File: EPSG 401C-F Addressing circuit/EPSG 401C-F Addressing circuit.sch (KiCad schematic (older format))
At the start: 4 parts, among them J1 Conn_01x16_Female, U1 74LS138, U2 74LS138, U3 74LS138

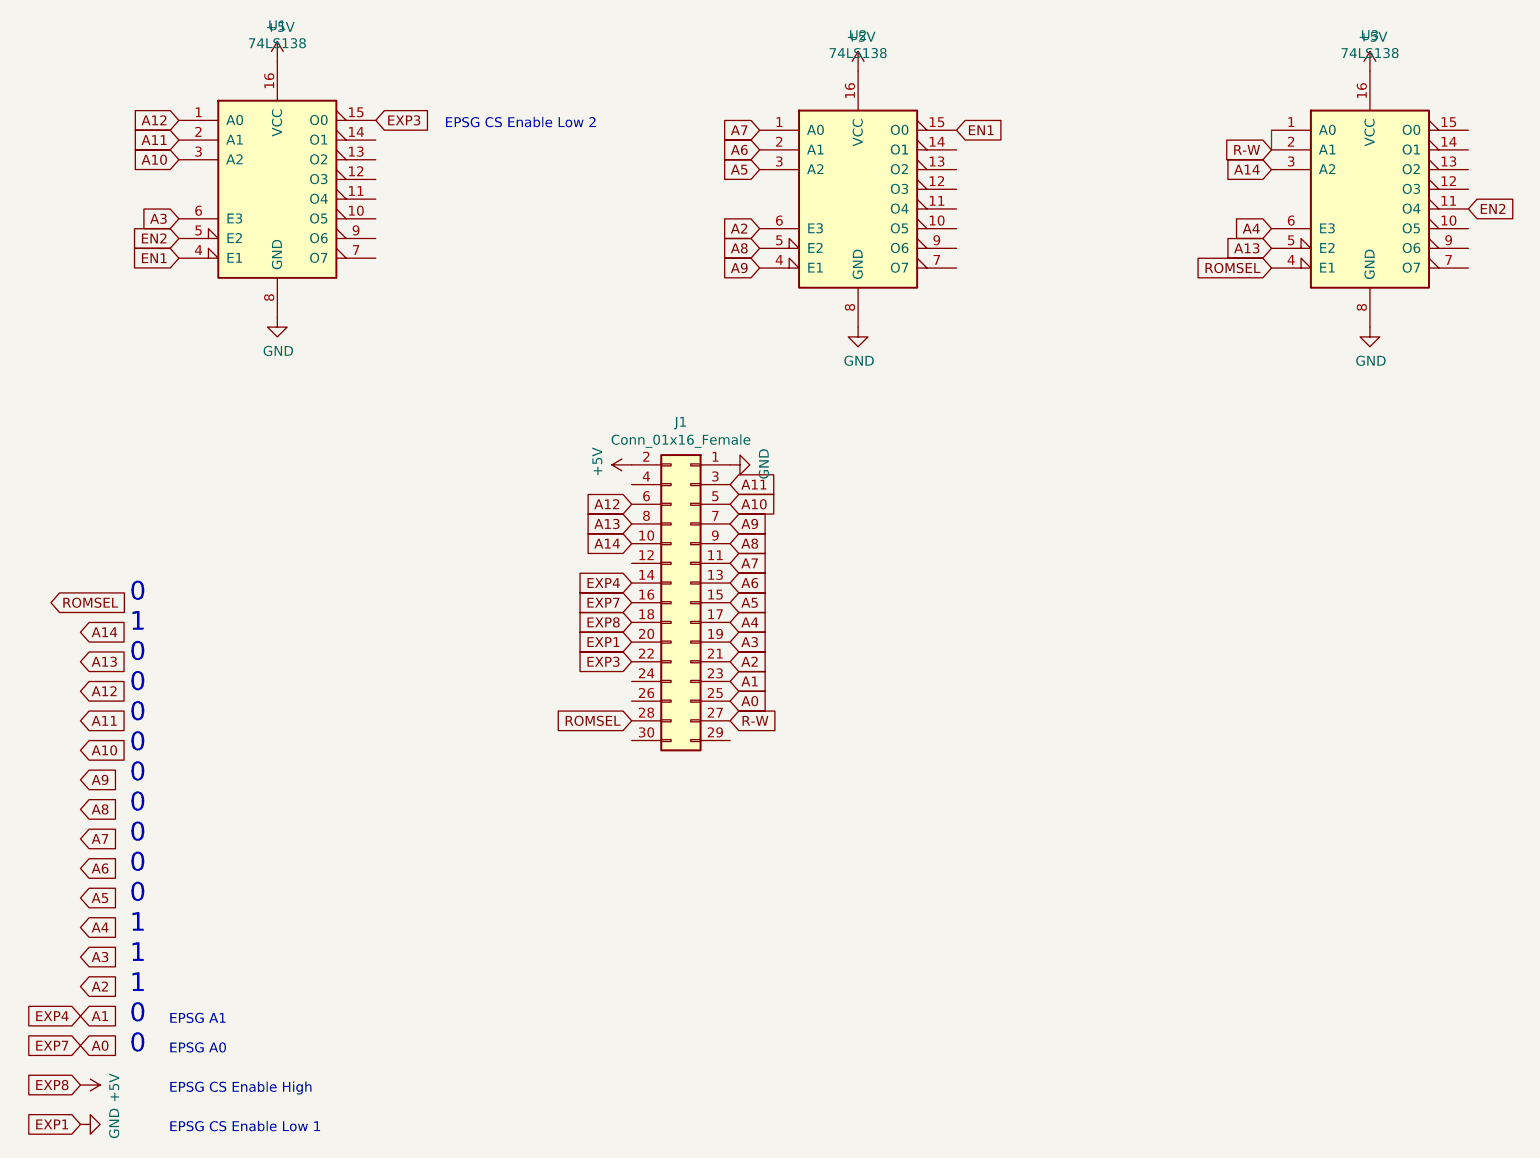
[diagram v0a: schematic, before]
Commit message: Added M2 to the addressing circuit and famicom daughterboard connector
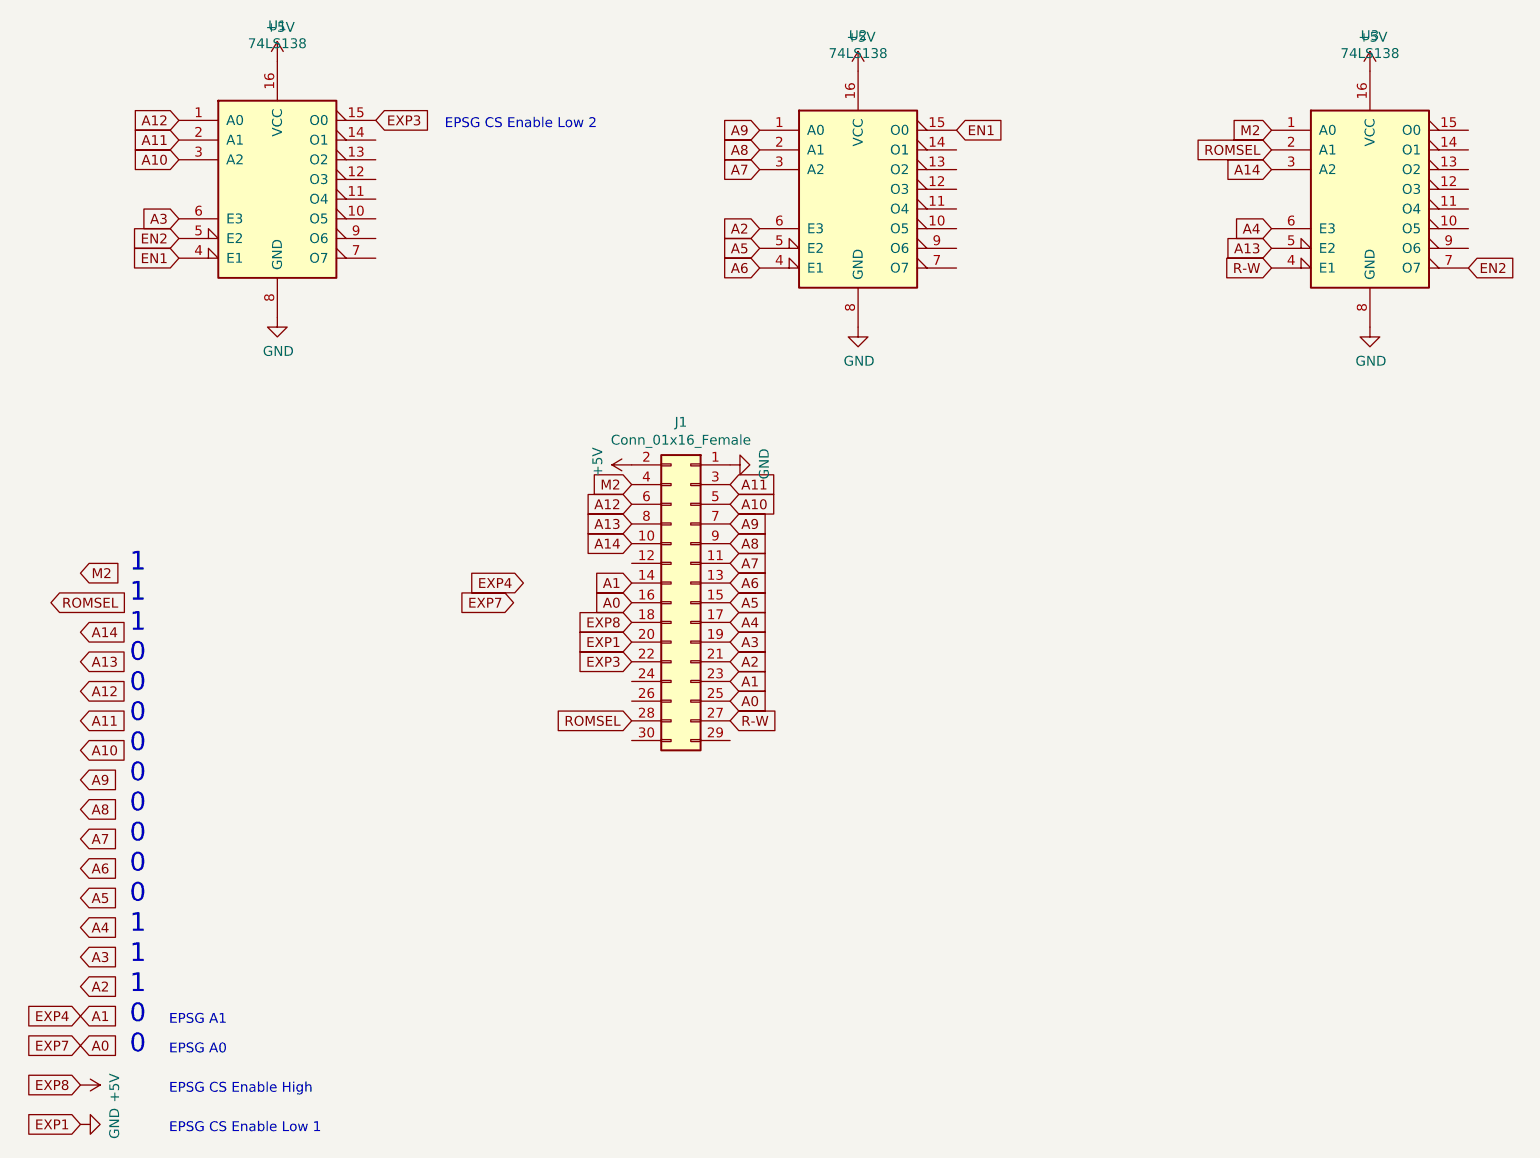
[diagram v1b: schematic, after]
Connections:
- net A5: now also U2.5 (E2); no longer U2.3 (A2)
- net A6: now also U2.4 (E1); no longer U2.2 (A1)
- net A7: now also U2.3 (A2); no longer U2.1 (A0)
- net A8: now also U2.2 (A1); no longer U2.5 (E2)
- net A9: now also U2.1 (A0); no longer U2.4 (E1)
- net EN2: now also U3.7 (O7); no longer U3.11 (O4)
- net R-W: now also U3.4 (E1); no longer U3.1 (A0), U3.2 (A1)
- net ROMSEL: now also U3.2 (A1); no longer U3.4 (E1)
- net M2: now reaches J1.4 (Pin_4)
- net M2: now also U3.1 (A0)
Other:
- note added: "1\n1\n1\n0\n0\n0\n0\n0\n0\n0\n0\n0\n1\n1\n1\n0\n0"
- note removed: "0\n1\n0\n0\n0\n0\n0\n0\n0\n0\n0\n1\n1\n1\n0\n0"
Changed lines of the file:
@@
 A9
 Text Notes 2150 6700 0    95   ~ 0
-0\n1\n0\n0\n0\n0\n0\n0\n0\n0\n0\n1\n1\n1\n0\n0
+1\n1\n1\n0\n0\n0\n0\n0\n0\n0\n0\n0\n1\n1\n1\n0\n0
 $Comp
 L 74xx:74LS138 U3
@@
 Text GLabel 7950 2500 0    50   Input ~ 0
 A4
-Text GLabel 5350 2200 0    50   Input ~ 0
+Text GLabel 5350 2600 0    50   Input ~ 0
 A5
-Text GLabel 5350 2100 0    50   Input ~ 0
+Text GLabel 5350 2700 0    50   Input ~ 0
 A6
 Text GLabel 5350 2000 0    50   Input ~ 0
-A7
-Text GLabel 5350 2600 0    50   Input ~ 0
-A8
-Text GLabel 5350 2700 0    50   Input ~ 0
 A9
 Text GLabel 2400 2150 0    50   Input ~ 0
 A10
-Text GLabel 2400 2050 0    50   Input ~ 0
-A11
 Text GLabel 2400 1950 0    50   Input ~ 0
 A12
@@
 Text GLabel 7950 2200 0    50   Input ~ 0
 A14
-Wire Wire Line
-	7950 2000 7950 2100
+Text GLabel 7950 2100 0    50   Input ~ 0
+ROMSEL
 Text GLabel 7950 2700 0    50   Input ~ 0
-ROMSEL
-Text GLabel 7950 2100 0    50   Input ~ 0
 R-W
 $Comp
@@
 Text GLabel 1750 4400 2    50   Input ~ 0
 ROMSEL
-Text GLabel 8950 2400 2    50   Input ~ 0
+Text GLabel 8950 2700 2    50   Input ~ 0
 EN2
 Text GLabel 2400 2550 0    50   Input ~ 0
@@
 Text GLabel 4700 5000 0    50   Input ~ 0
 ROMSEL
-Text GLabel 4700 4300 0    50   Input ~ 0
+Text GLabel 4150 4300 0    50   Input ~ 0
 EXP4
-Text GLabel 4700 4400 0    50   Input ~ 0
+Text GLabel 4100 4400 0    50   Input ~ 0
 EXP7
 Text GLabel 4700 4500 0    50   Input ~ 0
@@
 Text GLabel 4700 4700 0    50   Input ~ 0
 EXP3
+Text GLabel 5350 2100 0    50   Input ~ 0
+A8
+Text GLabel 2400 2050 0    50   Input ~ 0
+A11
+Text GLabel 5350 2200 0    50   Input ~ 0
+A7
+Text GLabel 4700 4300 0    50   Input ~ 0
+A1
+Text GLabel 4700 4400 0    50   Input ~ 0
+A0
+Text GLabel 1900 4250 2    50   Input ~ 0
+M2
+Text GLabel 7950 2000 0    50   Input ~ 0
+M2
+Text GLabel 4700 3800 0    50   Input ~ 0
+M2
 $EndSCHEMATC
